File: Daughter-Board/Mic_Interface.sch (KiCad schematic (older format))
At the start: 9 parts

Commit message: changed n-type MOSFETs to cd4016 plus minor changes
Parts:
- removed C?: 1uF, Capacitor_SMD:C_1206_3216Metric, symbol Device:C_Small
- removed P? (x2): Board_Edge_Conn, dcm-footprint:Edge_Conn, symbol dcm-symbols:Board_Edge_Conn
- removed R?: 100KΩ, Resistor_SMD:R_1206_3216Metric, symbol Device:R_US
- removed U? (x5): LMV934MA, Package_SO:TSSOP-14_4.4x5mm_P0.65mm, symbol Amplifier_Operational:LM324A
- added J301: Conn_01x08_0.5mm_Female_Kyocera, dcm-footprint:Kyocera_6288, symbol dcm-symbols:Conn_01x08_0.5mm_Female_Kyocera
- added R301, R305: 10KΩ, Resistor_SMD:R_1206_3216Metric, symbol Device:R_US
- added R302, R303, R306, R307: 100KΩ, Resistor_SMD:R_1206_3216Metric, symbol Device:R_US
- added U103: MC74VHCT126A, Package_SO:SOIC-14_3.9x8.7mm_P1.27mm, symbol 74xx:74LS126
- added U104, U108: 4016, symbol 4xxx:4016
- added U301: LM324A, Package_SO:TSSOP-14_4.4x5mm_P0.65mm, symbol Amplifier_Operational:LM324A
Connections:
- net labels added: AOut, CLK_EN, DOut, DOut_En, MST_CLK, NegEn, No_Gain, PlusEn, Plus_GND, Select, V_Bias, Word_Strobe
- net labels removed: +5V
- wire segments 82 -> 67
- no-connect marks 4 -> 2
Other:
- note added: "1. Need to place test points."
- note added: "GND"
- note added: "GND, WS"
- note added: "OUT (+), DATA"
- note added: "OUT (-), BIT CLK"
- note added: "PWR"
- note added: "SELECT"

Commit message: Add test points to Digital and Daughter-Board schematics
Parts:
- U102: renamed from U301; footprint Package_SO:TSSOP-14_4.4x5mm_P0.65mm -> Package_SO:SOIC-14_3.9x8.7mm_P1.27mm
- renumbered R305 to R304, R306 to R305, R307 to R306, U104 to U105, U103 to U107, U104 to U108
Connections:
- net AOut: now also U102.14; no longer U102.1
- net CLK_EN: now also U107.10; no longer U107.1
- net DOut: now also U108.10; no longer U108.2
- net DOut_En: now also U108.12; no longer U108.13
- net MST_CLK: now also U107.9; no longer U107.2
- net at R301.1, R303.2, U108.4: now also U102.12 (+); no longer U102.3 (+)
- net at R304.2, R305.2, U105.10: now also U102.13 (-); no longer U102.2 (-)
- net at J301.4 (Pin_4), U108.1: now also U108.11; no longer U108.1
- net at J301.5 (Pin_5), U108.8: now also U107.8; no longer U107.3
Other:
- note removed: "1. Need to place test points."

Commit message: Add DigiKey # or Mouser # to component info, update footprintinfo for 14 and 20 pin devices.
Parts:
- R301, R304: DigiKey # (none) -> 541-3983-1-ND
- R302: DigiKey # (none) -> 5414173-1-ND
- R303, R305: DigiKey # (none) -> 541-4173-1-ND
- U107: Mouser # (none) -> 771-74VHCT126D118
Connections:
- net AOut: now also U102.7, U105.4; no longer U102.14, U105.11
- net CLK_EN: now also U107.4; no longer U107.10
- net MST_CLK: now also U107.5; no longer U107.9
- net No_Gain: now also U105.5; no longer U105.12
- net at R301.1, R303.2, U108.4: now also U102.5 (+); no longer U102.12 (+)
- net at R304.2, R305.2: now also U102.6 (-), U105.3; no longer U102.13 (-), U105.10
- net at J301.5 (Pin_5), U108.8: now also U107.6; no longer U107.8
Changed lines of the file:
@@
 $Descr A4 11693 8268
 encoding utf-8
-Sheet 6 6
+Sheet 4 6
 Title "Daughter Board"
 Date ""
@@
 AR Path="/6159E578/612F28D7" Ref="R601"  Part="1"
 AR Path="/6159EF26/612F28D7" Ref="R501"  Part="1"
-F 0 "R601" V 6080 1900 50  0000 L CNN
+F 0 "R401" V 6080 1900 50  0000 L CNN
 F 1 "10KΩ" V 6160 1890 50  0000 L CNN
 F 2 "Resistor_SMD:R_1206_3216Metric" V 6290 1990 50  0001 C CNN
 F 3 "~" H 6250 2000 50  0001 C CNN
+F 4 "541-3983-1-ND" V 6250 2000 50  0001 C CNN "DigiKey #"
 	1    6250 2000
 	0    1    1    0
@@
 AR Path="/6159E578/612F28DD" Ref="R603"  Part="1"
 AR Path="/6159EF26/612F28DD" Ref="R503"  Part="1"
-F 0 "R603" H 7650 2520 50  0000 L CNN
+F 0 "R403" H 7650 2520 50  0000 L CNN
 F 1 "100KΩ" H 7630 2590 50  0000 L CNN
 F 2 "Resistor_SMD:R_1206_3216Metric" V 7940 2440 50  0001 C CNN
 F 3 "~" H 7900 2450 50  0001 C CNN
+F 4 "541-4173-1-ND" H 7900 2450 50  0001 C CNN "DigiKey #"
 	1    7900 2450
 	-1   0    0    1
@@
 $Comp
 L Amplifier_Operational:LM324A U?
-U 4 1 612F28EA
+U 2 1 612F28EA
 P 8410 2100
 AR Path="/612F28EA" Ref="U?"  Part="1"
@@
 F 2 "Package_SO:SOIC-14_3.9x8.7mm_P1.27mm" H 8360 2200 50  0001 C CNN
 F 3 "" H 8460 2300 50  0001 C CNN
-	4    8410 2100
+	2    8410 2100
 	1    0    0    -1
 $EndComp
@@
 AR Path="/6159E578/612F28F6" Ref="R605"  Part="1"
 AR Path="/6159EF26/612F28F6" Ref="R505"  Part="1"
-F 0 "R605" V 8580 3680 50  0000 L CNN
+F 0 "R405" V 8580 3680 50  0000 L CNN
 F 1 "100KΩ" V 8660 3660 50  0000 L CNN
 F 2 "Resistor_SMD:R_1206_3216Metric" V 8790 3790 50  0001 C CNN
 F 3 "~" H 8750 3800 50  0001 C CNN
+F 4 "541-4173-1-ND" V 8750 3800 50  0001 C CNN "DigiKey #"
 	1    8750 3800
 	0    1    1    0
@@
 AR Path="/6159E578/612F2915" Ref="R604"  Part="1"
 AR Path="/6159EF26/612F2915" Ref="R504"  Part="1"
-F 0 "R604" V 6890 3200 50  0000 L CNN
+F 0 "R404" V 6890 3200 50  0000 L CNN
 F 1 "10KΩ" V 6810 3190 50  0000 L CNN
 F 2 "Resistor_SMD:R_1206_3216Metric" V 7050 3290 50  0001 C CNN
 F 3 "~" H 7010 3300 50  0001 C CNN
+F 4 "541-3983-1-ND" V 7010 3300 50  0001 C CNN "DigiKey #"
 	1    7010 3300
 	0    -1   -1   0
@@
 AR Path="/6159E578/612F296B" Ref="#PWR0603"  Part="1"
 AR Path="/6159EF26/612F296B" Ref="#PWR0503"  Part="1"
-F 0 "#PWR0603" H 7000 2660 50  0001 C CNN
+F 0 "#PWR0403" H 7000 2660 50  0001 C CNN
 F 1 "GNDREF" H 7005 2737 50  0001 C CNN
 F 2 "" H 7000 2910 50  0001 C CNN
@@
 AR Path="/6159E578/612F29B8" Ref="#PWR0601"  Part="1"
 AR Path="/6159EF26/612F29B8" Ref="#PWR0501"  Part="1"
-F 0 "#PWR0601" H 4810 1450 50  0001 C CNN
+F 0 "#PWR0401" H 4810 1450 50  0001 C CNN
 F 1 "GNDREF" H 4815 1527 50  0001 C CNN
 F 2 "" H 4810 1700 50  0001 C CNN
@@
 $Comp
 L 74xx:74LS126 U?
-U 3 1 612F29C2
+U 2 1 612F29C2
 P 6300 5500
 AR Path="/60E235BF/612F29C2" Ref="U?"  Part="1"
@@
 F 2 "Package_SO:SOIC-14_3.9x8.7mm_P1.27mm" H 6300 5500 50  0001 C CNN
 F 3 "" H 6300 5500 50  0001 C CNN
-	3    6300 5500
+F 4 "771-74VHCT126D118" H 6300 5500 50  0001 C CNN "Mouser #"
+	2    6300 5500
 	-1   0    0    -1
 $EndComp
@@
 AR Path="/6159E578/6151F074" Ref="R606"  Part="1"
 AR Path="/6159EF26/6151F074" Ref="R506"  Part="1"
-F 0 "R606" H 6220 4230 50  0000 L CNN
+F 0 "R406" H 6220 4230 50  0000 L CNN
 F 1 "100KΩ" H 6190 4300 50  0000 L CNN
 F 2 "Resistor_SMD:R_1206_3216Metric" V 6540 4240 50  0001 C CNN
@@
 AR Path="/6159E578/61527AC0" Ref="R602"  Part="1"
 AR Path="/6159EF26/61527AC0" Ref="R502"  Part="1"
-F 0 "R602" V 5660 2300 50  0000 L CNN
+F 0 "R402" V 5660 2300 50  0000 L CNN
 F 1 "100KΩ" V 5740 2270 50  0000 L CNN
 F 2 "Resistor_SMD:R_1206_3216Metric" V 5890 2390 50  0001 C CNN
 F 3 "~" H 5850 2400 50  0001 C CNN
+F 4 "5414173-1-ND" V 5850 2400 50  0001 C CNN "DigiKey #"
 	1    5850 2400
 	0    1    1    0
@@
 AR Path="/6159E578/6152B7FD" Ref="#PWR0602"  Part="1"
 AR Path="/6159EF26/6152B7FD" Ref="#PWR0502"  Part="1"
-F 0 "#PWR0602" H 6200 2350 50  0001 C CNN
+F 0 "#PWR0402" H 6200 2350 50  0001 C CNN
 F 1 "GNDREF" H 6205 2427 50  0001 C CNN
 F 2 "" H 6200 2600 50  0001 C CNN
@@
 AR Path="/6159E578/6159108D" Ref="#PWR0605"  Part="1"
 AR Path="/6159EF26/6159108D" Ref="#PWR0505"  Part="1"
-F 0 "#PWR0605" H 6500 4350 50  0001 C CNN
+F 0 "#PWR0405" H 6500 4350 50  0001 C CNN
 F 1 "GNDREF" H 6505 4427 50  0001 C CNN
 F 2 "" H 6500 4600 50  0001 C CNN
@@
 AR Path="/6159E578/612F293F" Ref="J601"  Part="1"
 AR Path="/6159EF26/612F293F" Ref="J501"  Part="1"
-F 0 "J601" H 4210 2600 50  0000 L CNN
+F 0 "J401" H 4210 2600 50  0000 L CNN
 F 1 "Conn_01x08_0.5mm_Female_Kyocera" H 3650 1570 50  0001 L CNN
 F 2 "dcm-footprint:Kyocera_6288" H 4410 2100 50  0001 C CNN
@@
 AR Path="/6159EF26/615B1C2B" Ref="U103"  Part="1"
 AR Path="/6159E578/615B1C2B" Ref="U104"  Part="1"
-F 0 "U104" H 5510 1770 50  0000 C CNN
+F 0 "U109" H 5510 1770 50  0000 C CNN
 F 1 "4016" H 5500 1860 50  0000 C CNN
 F 2 "" H 5500 2000 50  0001 C CNN
@@
 AR Path="/6159EF26/615B2703" Ref="U103"  Part="2"
 AR Path="/6159E578/615B2703" Ref="U104"  Part="2"
-F 0 "U104" V 6954 2372 50  0000 R CNN
+F 0 "U109" V 6954 2372 50  0000 R CNN
 F 1 "4016" V 7045 2372 50  0000 R CNN
 F 2 "" H 7000 2500 50  0001 C CNN
@@
 AR Path="/6159EF26/615B41E1" Ref="U103"  Part="3"
 AR Path="/6159E578/615B41E1" Ref="U104"  Part="3"
-F 0 "U104" H 6000 3070 50  0000 C CNN
+F 0 "U109" H 6000 3070 50  0000 C CNN
 F 1 "4016" H 6000 3160 50  0000 C CNN
 F 2 "" H 6000 3300 50  0001 C CNN
@@
 $Comp
 L 4xxx:4016 U105
-U 4 1 615B5217
+U 2 1 615B5217
 P 8700 4200
 AR Path="/612D7BBA/615B5217" Ref="U105"  Part="1"
@@
 F 2 "" H 8700 4200 50  0001 C CNN
 F 3 "http://www.ti.com/lit/ds/symlink/cd4016b.pdf" H 8700 4200 50  0001 C CNN
-	4    8700 4200
+	2    8700 4200
 	-1   0    0    1
 $EndComp
@@
 AR Path="/6159E578/61655223" Ref="#PWR0604"  Part="1"
 AR Path="/6159EF26/61655223" Ref="#PWR0504"  Part="1"
-F 0 "#PWR0604" H 7900 2660 50  0001 C CNN
+F 0 "#PWR0404" H 7900 2660 50  0001 C CNN
 F 1 "GNDREF" H 7905 2737 50  0001 C CNN
 F 2 "" H 7900 2910 50  0001 C CNN
@@
 AR Path="/6159EF26/615D07EE" Ref="U103"  Part="4"
 AR Path="/6159E578/615D07EE" Ref="U104"  Part="4"
-F 0 "U104" H 6210 1170 50  0000 C CNN
+F 0 "U109" H 6210 1170 50  0000 C CNN
 F 1 "4016" H 6200 1260 50  0000 C CNN
 F 2 "" H 6200 1400 50  0001 C CNN

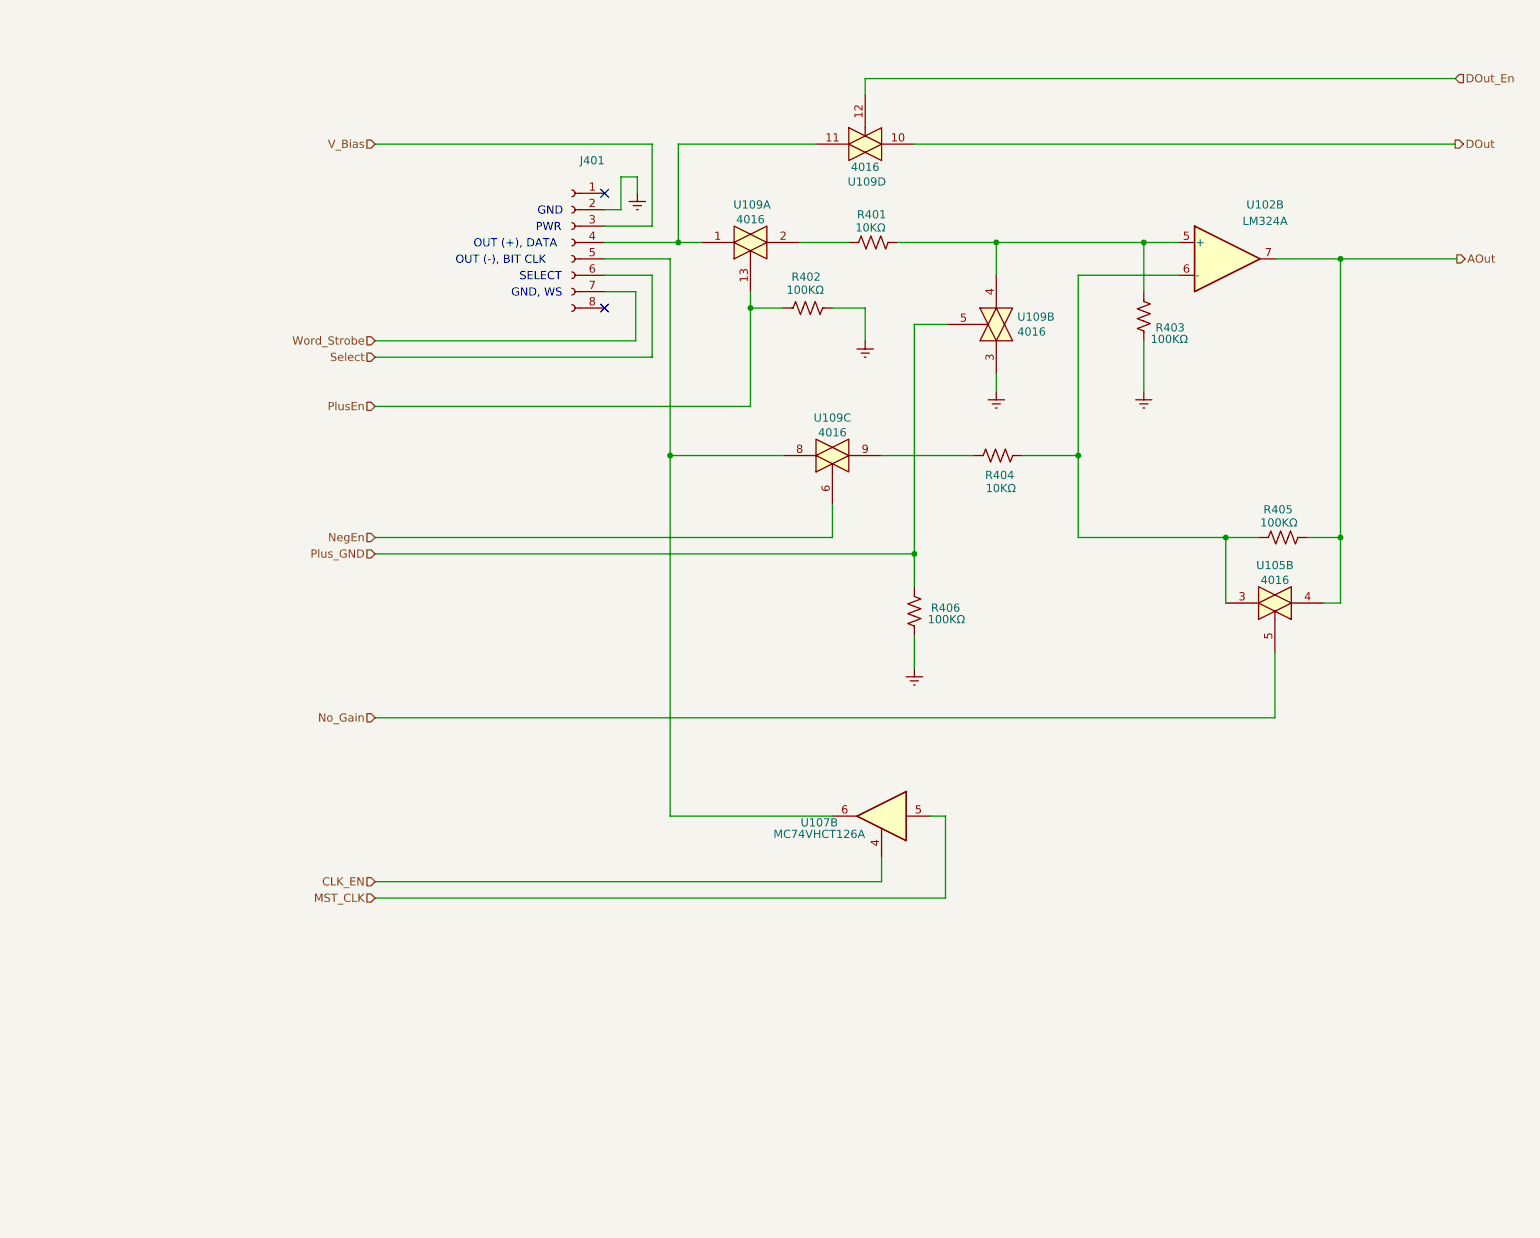
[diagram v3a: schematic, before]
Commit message: Corrected analog gain switch position.
Analog gain switch was across the feedback resistor. It is changed to grounding of the - input resistor to the op amp.
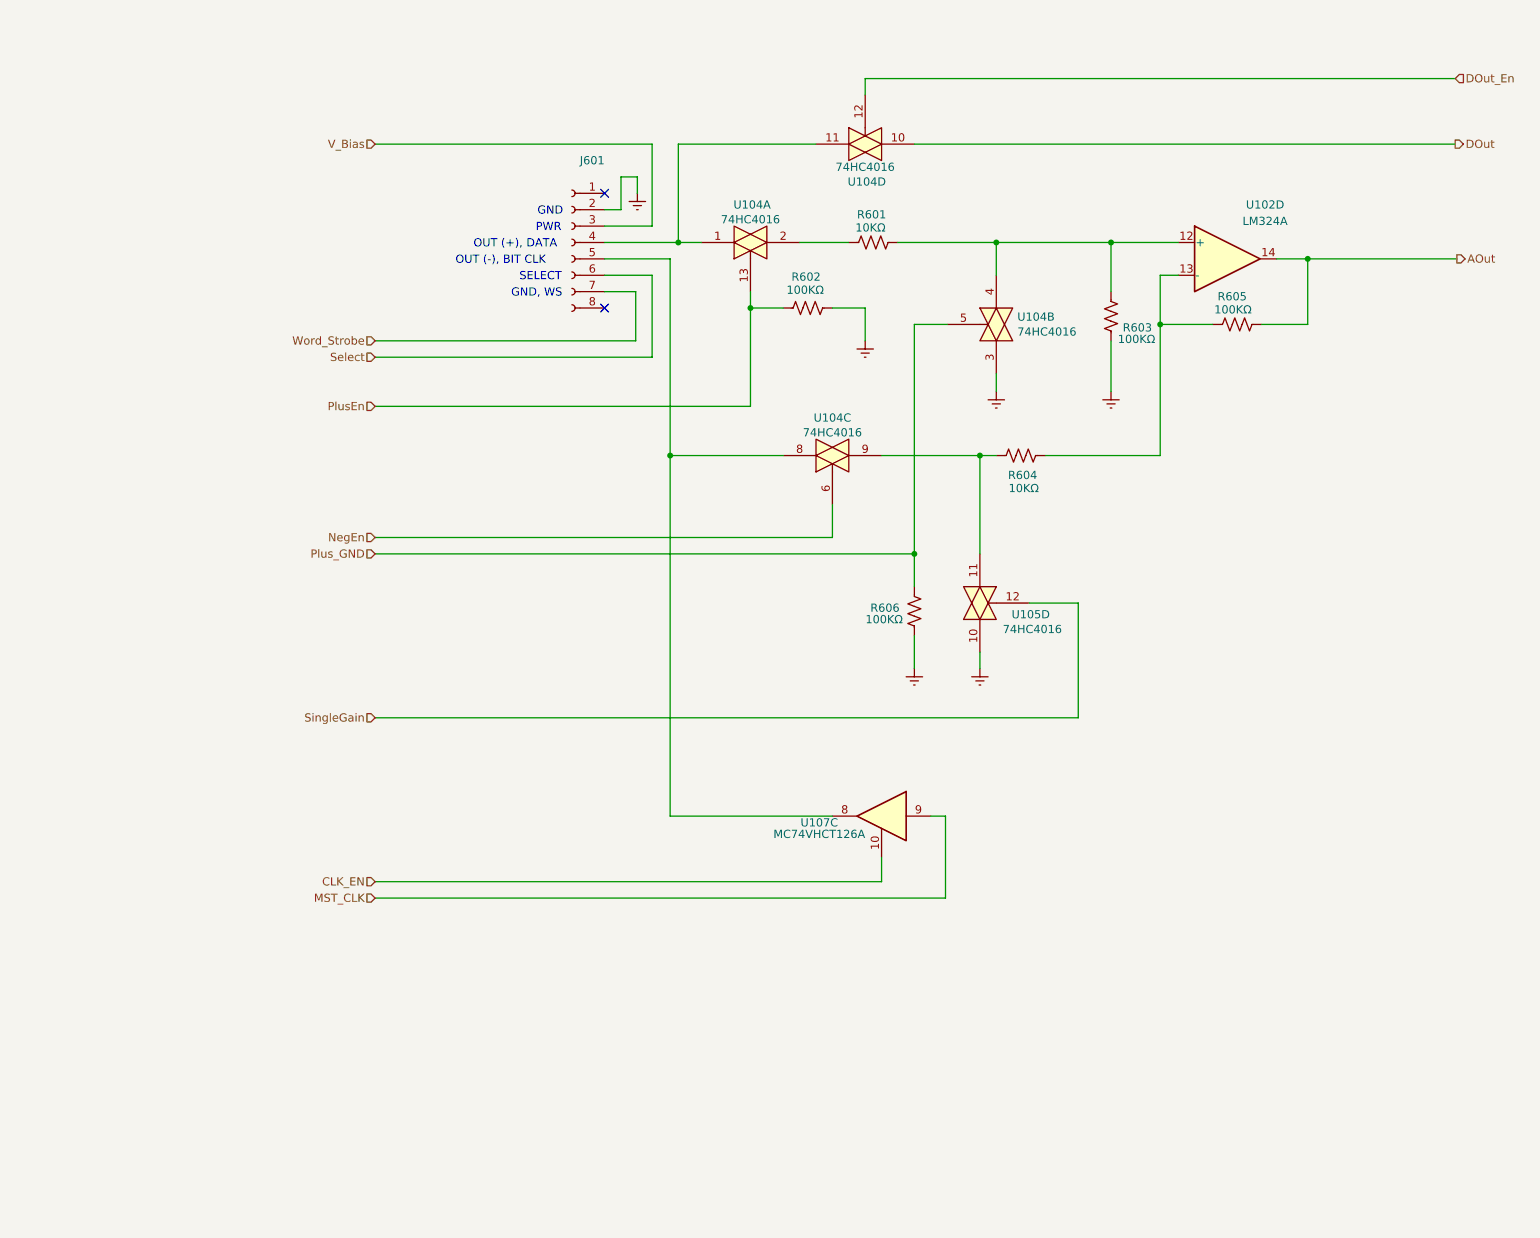
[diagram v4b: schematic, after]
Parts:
- U105, U108: value 4016 -> 74HC4016
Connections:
- net AOut: now also U102.14; no longer U102.7, U105.4
- net CLK_EN: now also U107.10; no longer U107.4
- net GNDREF: now also U105.10
- net MST_CLK: now also U107.9; no longer U107.5
- net at R301.1, R303.2, U108.4: now also U102.12 (+); no longer U102.5 (+)
- net at R304.2, R305.2: now also U102.13 (-); no longer U102.6 (-), U105.3
- net at R304.1, U108.9: now also U105.11
- net at J301.5 (Pin_5), U108.8: now also U107.8; no longer U107.6
- removed net No_Gain: U105.5
- new net SingleGain: U105.12
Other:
- moved on the sheet: R603, R604, R605

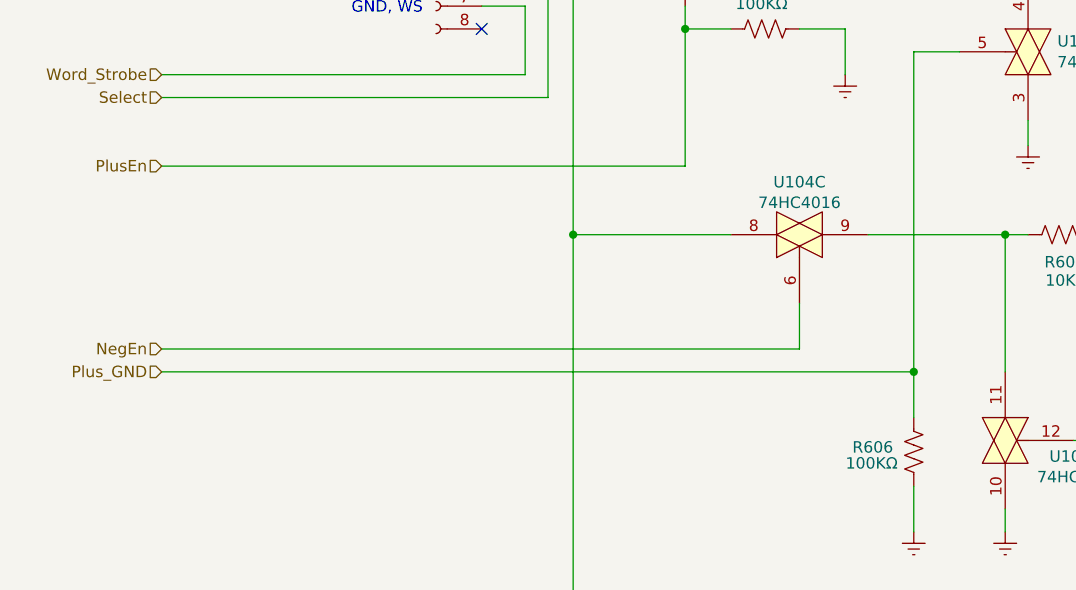
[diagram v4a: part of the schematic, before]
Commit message: Remove LEDs and circuitry, update J201 footprint to have a square pad on pin 1.]
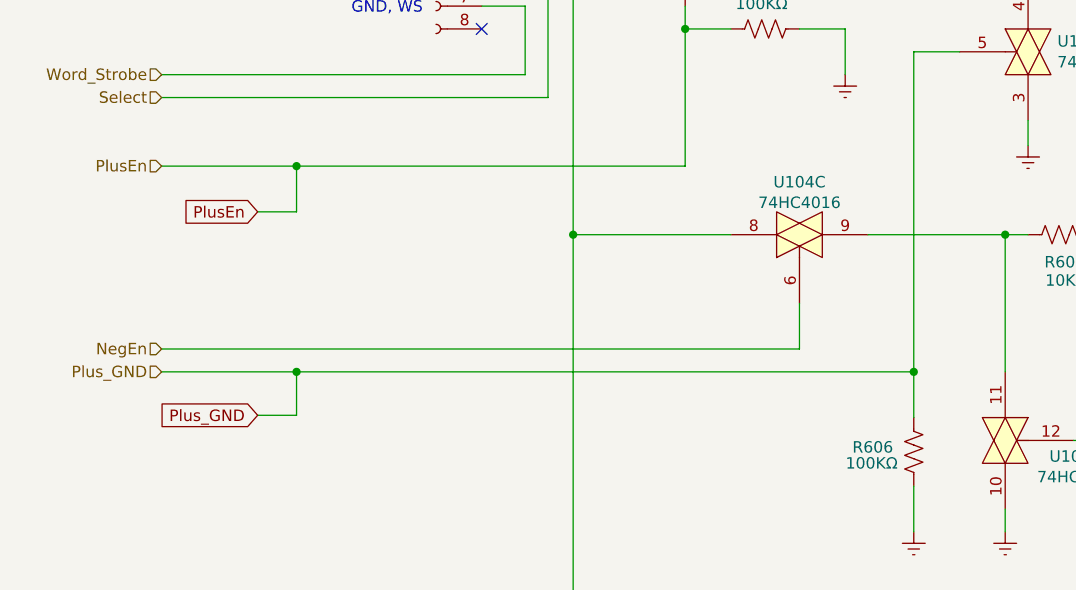
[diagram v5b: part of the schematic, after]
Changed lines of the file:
@@
 	6600 5500 6690 5500
-Wire Wire Line
-	6500 3900 3210 3900
 Wire Wire Line
 	5800 2000 6100 2000
@@
 $EndComp
 Wire Wire Line
-	5500 3000 3210 3000
+	5500 3000 3800 3000
 Wire Wire Line
 	5500 2400 5700 2400
@@
 Wire Wire Line
 	8900 2100 9810 2100
+Text GLabel 3630 4090 0    50   Input ~ 0
+Plus_GND
+Wire Wire Line
+	3210 3900 3800 3900
+Wire Wire Line
+	3630 4090 3800 4090
+Wire Wire Line
+	3800 4090 3800 3900
+Connection ~ 3800 3900
+Wire Wire Line
+	3800 3900 6500 3900
+Text GLabel 3630 3200 0    50   Input ~ 0
+PlusEn
+Wire Wire Line
+	3630 3200 3800 3200
+Wire Wire Line
+	3800 3200 3800 3000
+Connection ~ 3800 3000
+Wire Wire Line
+	3800 3000 3210 3000
 $EndSCHEMATC
